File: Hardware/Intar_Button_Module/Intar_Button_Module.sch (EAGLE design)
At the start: 19 parts, among them J1 GROVE-4P-2.0-3470130P1, Q1 MMBT2222A, Q2 MMBT2222A

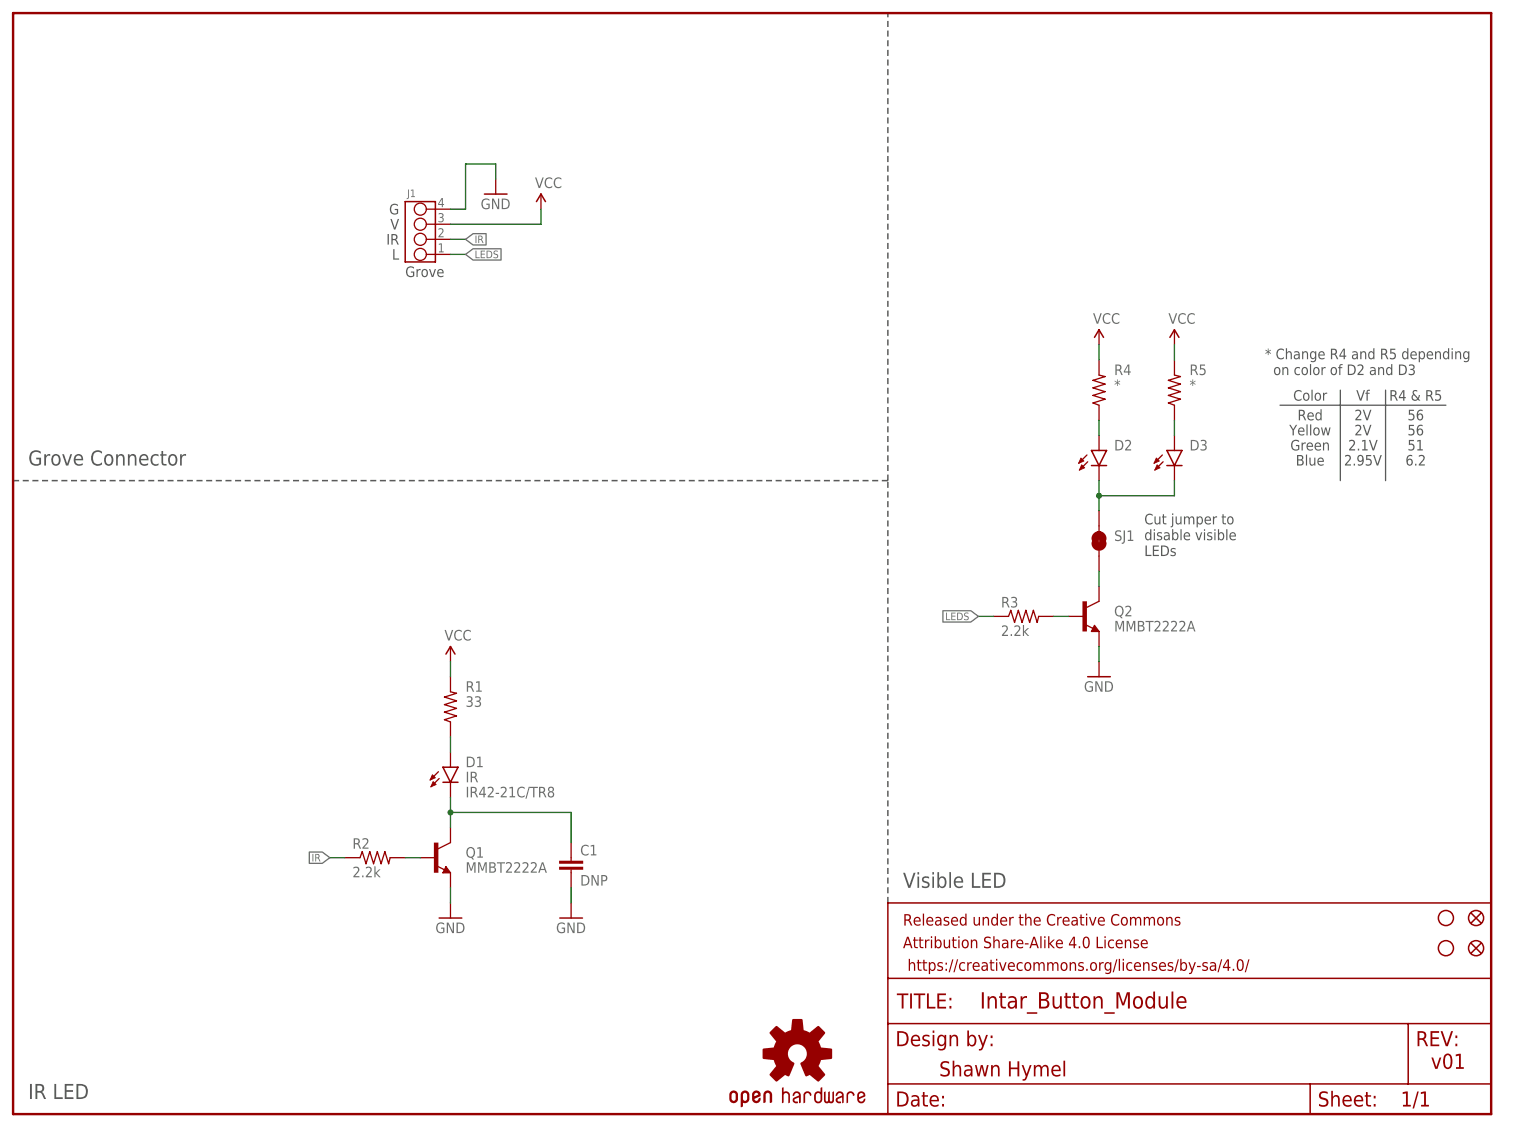
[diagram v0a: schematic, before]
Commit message: Created LP5521 part
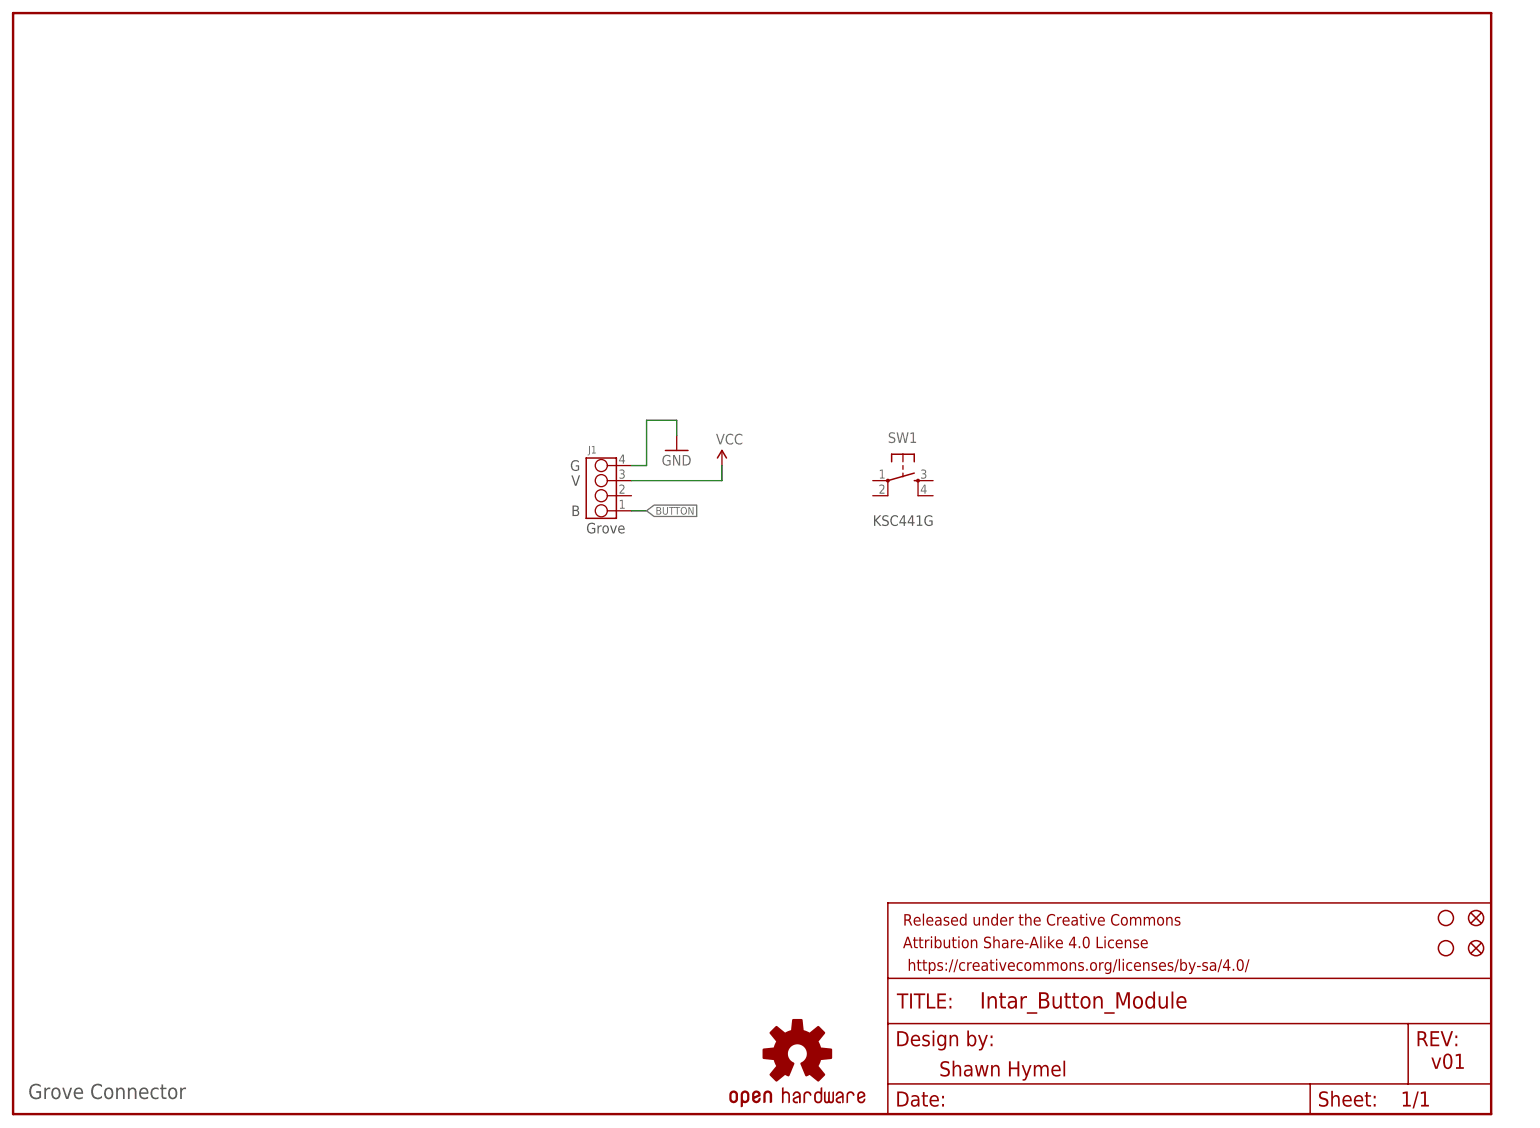
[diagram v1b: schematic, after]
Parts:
- removed C1: DNP, SparkFun-Capacitors:10NF/10000PF-50V-10%(0603)
- removed D1: IR, Intar_Eagle_Library:LEDIR42-21C/TR8
- removed D2, D3: (no value), SparkFun-LED:LED0603
- removed Q1, Q2: MMBT2222A, SparkFun-DiscreteSemi:TRANSISTOR_NPNMMBT2222A
- removed R1: 33, SparkFun-Resistors:RESISTOR0603-RES
- removed R2, R3: 2.2k, SparkFun-Resistors:2.2KOHM-1/10W-1%(0603)
- removed R4, R5: *, SparkFun-Resistors:RESISTOR0603-RES
- removed SJ1: JUMPER-PAD-2-NC_BY_TRACE, SparkFun-Passives:JUMPER-PAD-2-NC_BY_TRACE
- added SW1: SWITCH_MOMENTARY, Intar_Eagle_Library:SWITCH_MOMENTARY
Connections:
- removed net IR: J1.2, R2.1
- removed net LEDS: J1.1, R3.1
- removed net N$1: Q1.B, R2.2
- removed net N$2: D1.A, R1.1
- removed net N$3: C1.1, D1.C, Q1.C
- removed net N$4: D2.C, D3.C, SJ1.2
- removed net N$5: Q2.B, R3.2
- removed net N$6: D2.A, R4.1
- removed net N$7: D3.A, R5.1
- removed net N$8: Q2.C, SJ1.1
- new net BUTTON: J1.1
- net GND: no longer C1.2, Q1.E, Q2.E
- net VCC: no longer R1.2, R4.2, R5.2
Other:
- note added: "B"
- note added: "KSC441G"
- note removed: "* Change R4 and R5 depending on color of D2 and D3"
- note removed: "2.1V"
- note removed: "2.95V"
- note removed: "2V"
- note removed: "51"
- note removed: "56"
- note removed: "6.2"
- note removed: "Blue"
- note removed: "Color"
- note removed: "Cut jumper to disable visible LEDs"
- note removed: "Green"
- note removed: "IR"
- note removed: "IR LED"
- note removed: "L"
- note removed: "R4 & R5"
- note removed: "Red"
- note removed: "Vf"
- note removed: "Visible LED"
- note removed: "Yellow"
- moved on the sheet: J1
